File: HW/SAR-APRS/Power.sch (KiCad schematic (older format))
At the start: 22 parts

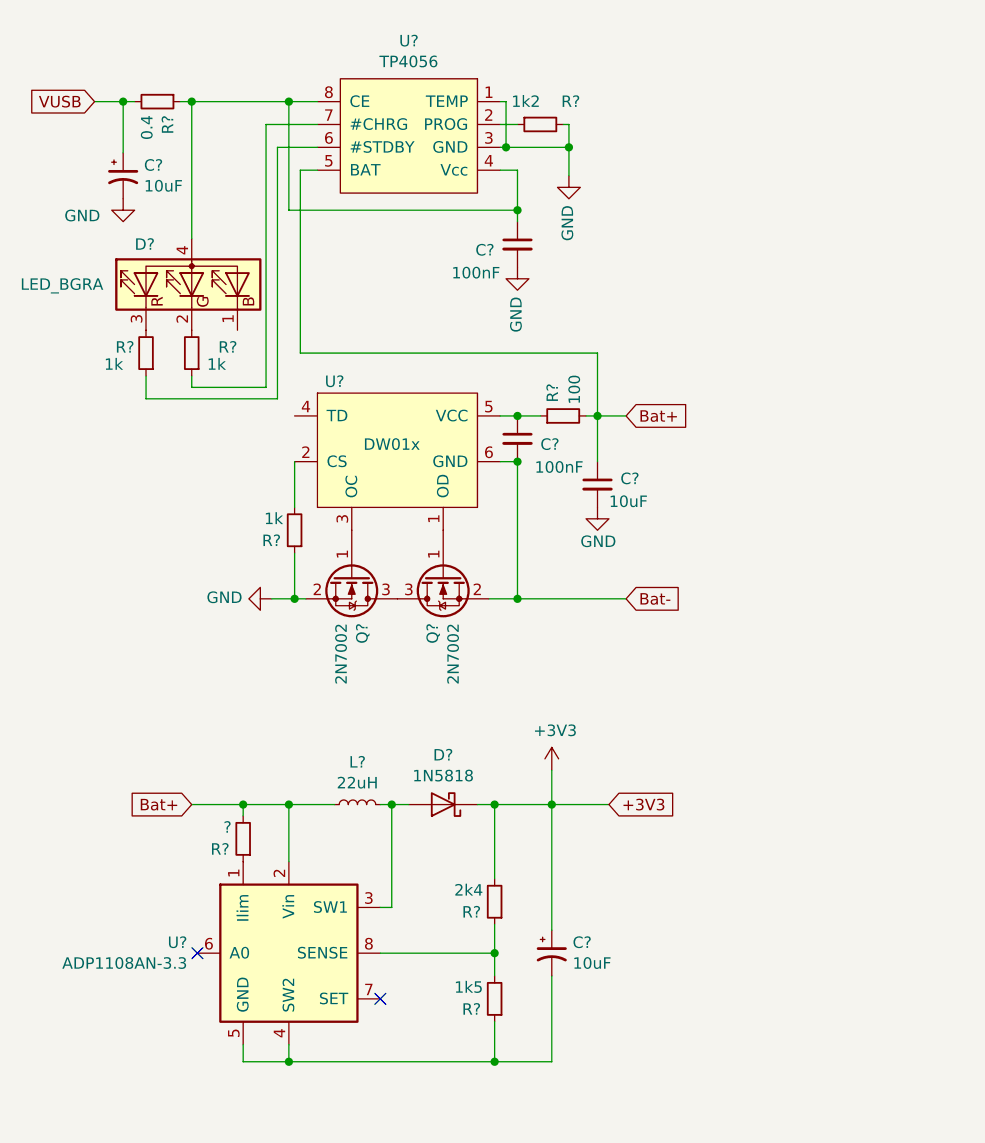
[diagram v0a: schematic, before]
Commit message: schematic update
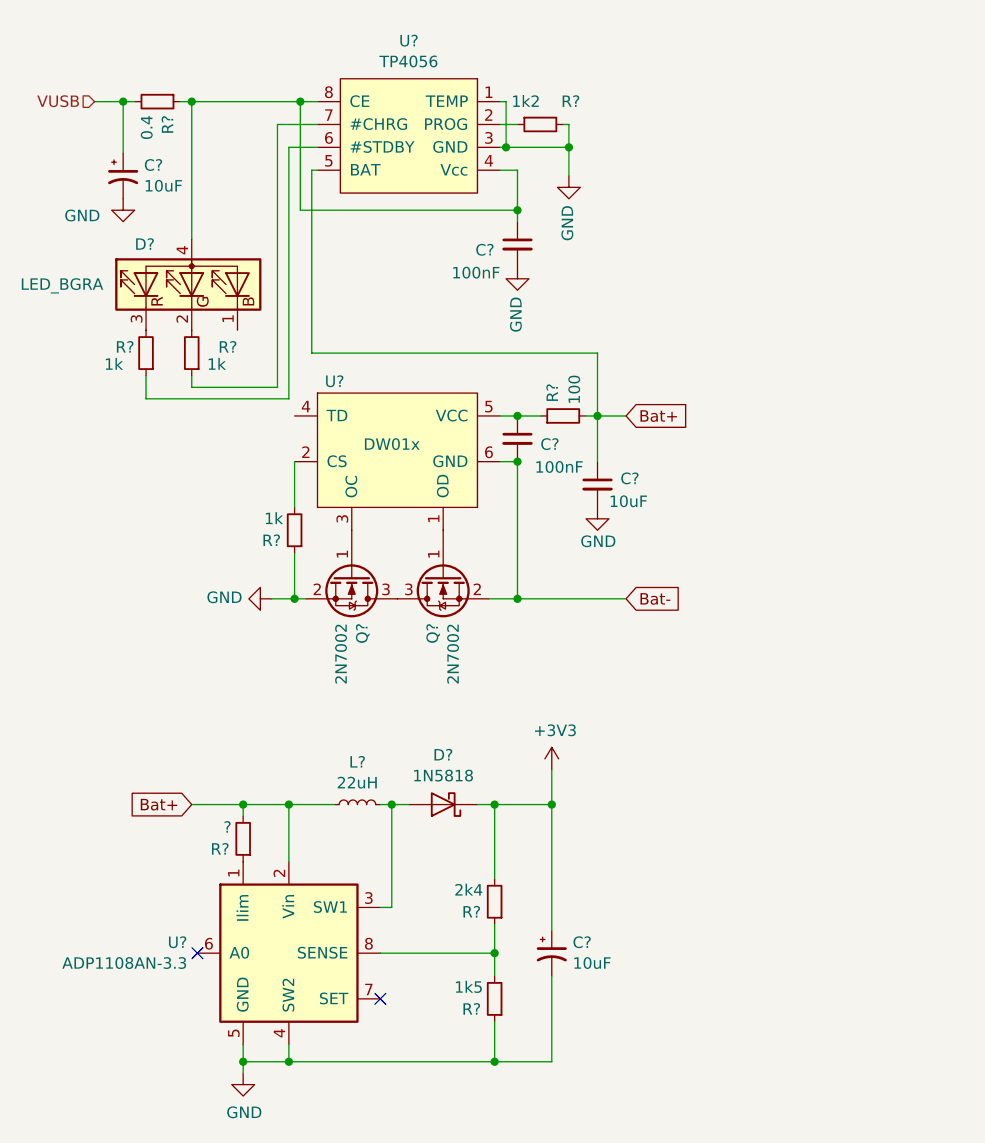
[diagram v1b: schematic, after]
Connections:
- net GND: now also C?.2, R?.1, U?.4 (SW2), U?.5 (GND)
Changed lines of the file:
@@
 	5050 3075 5050 3125
 Wire Wire Line
-	5050 3125 5375 3125
-Wire Wire Line
-	5375 1975 5600 1975
+	5050 3125 5425 3125
+Wire Wire Line
+	5425 1975 5600 1975
 Wire Wire Line
 	4850 3075 4850 3175
 Wire Wire Line
-	4850 3175 5425 3175
-Wire Wire Line
-	5425 2075 5600 2075
+	4850 3175 5475 3175
+Wire Wire Line
+	5475 2075 5600 2075
 $Comp
 L device:C_Small C?
@@
 $EndComp
 Wire Wire Line
-	5050 1875 5475 1875
-Wire Wire Line
-	5375 1975 5375 3125
-Wire Wire Line
-	5425 2075 5425 3175
-Wire Wire Line
-	5475 1875 5475 2350
-Wire Wire Line
-	5475 2350 6475 2350
-Wire Wire Line
-	5475 1875 5600 1875
+	5050 1875 5525 1875
+Wire Wire Line
+	5425 1975 5425 3125
+Wire Wire Line
+	5475 2075 5475 3175
+Wire Wire Line
+	5525 1875 5525 2350
+Wire Wire Line
+	5525 2350 6475 2350
+Wire Wire Line
+	5525 1875 5600 1875
 Wire Wire Line
 	6475 2175 6475 2350
@@
 Wire Wire Line
 	6700 2075 6700 2200
-Connection ~ 5475 1875
-Wire Wire Line
-	5600 2175 5525 2175
-Wire Wire Line
-	5525 2175 5525 2975
-Wire Wire Line
-	5525 2975 6825 2975
+Connection ~ 5525 1875
+Wire Wire Line
+	5600 2175 5575 2175
+Wire Wire Line
+	5575 2175 5575 2975
+Wire Wire Line
+	5575 2975 6825 2975
 Wire Wire Line
 	6825 2975 6825 3250
@@
 Text GLabel 5050 4950 0    50   Input ~ 0
 Bat+
-Text GLabel 4625 1875 0    50   Input ~ 0
-VUSB
 Wire Wire Line
 	4750 1875 4625 1875
 Connection ~ 4750 1875
-Text GLabel 6875 4950 2    50   Input ~ 0
-+3V3
-Wire Wire Line
-	6875 4950 6625 4950
+$Comp
+L power:GND #PWR?
+U 1 1 5C75CEA2
+P 5275 6125
+F 0 "#PWR?" H 5275 5875 50  0001 C CNN
+F 1 "GND" H 5280 5952 50  0000 C CNN
+F 2 "" H 5275 6125 50  0001 C CNN
+F 3 "" H 5275 6125 50  0001 C CNN
+	1    5275 6125
+	1    0    0    -1
+$EndComp
+Wire Wire Line
+	5275 6125 5275 6075
+Connection ~ 5275 6075
+Text HLabel 4625 1875 0    50   Input ~ 0
+VUSB
 $EndSCHEMATC

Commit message: schem and pcb update
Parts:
- R6: renamed from R?; footprint (none) -> Resistors_SMD:R_0805_HandSoldering
- R7: renamed from R?; footprint (none) -> Resistors_SMD:R_0603
- U2: renamed from U?; footprint (none) -> IO:SO-8_3.9x4.9mm_P1.27mm
- U3: renamed from U?; footprint (none) -> Mlab_IO:SOT-23-6
- U4: renamed from U?; footprint Housings_DIP:DIP-8_W7.62mm -> Housings_SOIC:SOIC-8_3.9x4.9mm_Pitch1.27mm
- gave numbers to parts that had none: 17
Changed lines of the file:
@@
 EESchema Schematic File Version 4
 LIBS:SAR-APRS-cache
-EELAYER 28 0
+EELAYER 29 0
 EELAYER END
 $Descr A4 11693 8268
@@
 P 6700 2200
 AR Path="/5C95AC3C" Ref="#PWR?"  Part="1"
-AR Path="/5C948828/5C95AC3C" Ref="#PWR?"  Part="1"
-F 0 "#PWR?" H 6700 1950 50  0001 C CNN
+AR Path="/5C948828/5C95AC3C" Ref="#PWR0115"  Part="1"
+F 0 "#PWR0115" H 6700 1950 50  0001 C CNN
 F 1 "GND" V 6705 2072 50  0000 R CNN
 F 2 "" H 6700 2200 50  0001 C CNN
@@
 P 6575 1975
 AR Path="/5C95AC42" Ref="R?"  Part="1"
-AR Path="/5C948828/5C95AC42" Ref="R?"  Part="1"
-F 0 "R?" V 6475 1800 50  0000 L CNN
+AR Path="/5C948828/5C95AC42" Ref="R7"  Part="1"
+F 0 "R7" V 6475 1800 50  0000 L CNN
 F 1 "1k2" V 6475 1975 50  0000 L CNN
-F 2 "" H 6575 1975 50  0001 C CNN
+F 2 "Resistors_SMD:R_0603" H 6575 1975 50  0001 C CNN
 F 3 "~" H 6575 1975 50  0001 C CNN
 	1    6575 1975
@@
 P 6825 3550
 AR Path="/5C95AC48" Ref="C?"  Part="1"
-AR Path="/5C948828/5C95AC48" Ref="C?"  Part="1"
-F 0 "C?" H 6925 3575 50  0000 L CNN
+AR Path="/5C948828/5C95AC48" Ref="C11"  Part="1"
+F 0 "C11" H 6925 3575 50  0000 L CNN
 F 1 "10uF" H 6875 3475 50  0000 L CNN
 F 2 "" H 6825 3550 50  0001 C CNN
@@
 P 4900 1875
 AR Path="/5C95AC4E" Ref="R?"  Part="1"
-AR Path="/5C948828/5C95AC4E" Ref="R?"  Part="1"
-F 0 "R?" H 4959 1921 50  0000 L CNN
+AR Path="/5C948828/5C95AC4E" Ref="R6"  Part="1"
+F 0 "R6" H 4959 1921 50  0000 L CNN
 F 1 "0.4" H 4959 1830 50  0000 L CNN
-F 2 "" H 4900 1875 50  0001 C CNN
+F 2 "Resistors_SMD:R_0805_HandSoldering" H 4900 1875 50  0001 C CNN
 F 3 "~" H 4900 1875 50  0001 C CNN
 	1    4900 1875
@@
 P 4750 2300
 AR Path="/5C95AC5E" Ref="#PWR?"  Part="1"
-AR Path="/5C948828/5C95AC5E" Ref="#PWR?"  Part="1"
-F 0 "#PWR?" H 4750 2050 50  0001 C CNN
+AR Path="/5C948828/5C95AC5E" Ref="#PWR0116"  Part="1"
+F 0 "#PWR0116" H 4750 2050 50  0001 C CNN
 F 1 "GND" H 4650 2225 50  0000 R CNN
 F 2 "" H 4750 2300 50  0001 C CNN
@@
 P 5050 2975
 AR Path="/5C95AC6D" Ref="R?"  Part="1"
-AR Path="/5C948828/5C95AC6D" Ref="R?"  Part="1"
-F 0 "R?" H 4850 2950 50  0000 L CNN
+AR Path="/5C948828/5C95AC6D" Ref="R9"  Part="1"
+F 0 "R9" H 4850 2950 50  0000 L CNN
 F 1 "1k" H 4900 3025 50  0000 L CNN
 F 2 "" H 5050 2975 50  0001 C CNN
@@
 P 4850 2975
 AR Path="/5C95AC73" Ref="R?"  Part="1"
-AR Path="/5C948828/5C95AC73" Ref="R?"  Part="1"
-F 0 "R?" H 4900 2950 50  0000 L CNN
+AR Path="/5C948828/5C95AC73" Ref="R8"  Part="1"
+F 0 "R8" H 4900 2950 50  0000 L CNN
 F 1 "1k" H 4950 3025 50  0000 L CNN
 F 2 "" H 4850 2975 50  0001 C CNN
@@
 P 5050 2675
 AR Path="/5C95AC7B" Ref="D?"  Part="1"
-AR Path="/5C948828/5C95AC7B" Ref="D?"  Part="1"
-F 0 "D?" V 5225 2925 50  0000 R CNN
+AR Path="/5C948828/5C95AC7B" Ref="D1"  Part="1"
+F 0 "D1" V 5225 2925 50  0000 R CNN
 F 1 "LED_BGRA" V 5050 3425 50  0000 R CNN
 F 2 "" H 5050 2625 50  0001 C CNN
@@
 P 6475 3350
 AR Path="/5C95AC89" Ref="C?"  Part="1"
-AR Path="/5C948828/5C95AC89" Ref="C?"  Part="1"
-F 0 "C?" H 6575 3325 50  0000 L CNN
+AR Path="/5C948828/5C95AC89" Ref="C10"  Part="1"
+F 0 "C10" H 6575 3325 50  0000 L CNN
 F 1 "100nF" H 6550 3225 50  0000 L CNN
 F 2 "" H 6475 3350 50  0001 C CNN
@@
 P 6675 3250
 AR Path="/5C95AC8F" Ref="R?"  Part="1"
-AR Path="/5C948828/5C95AC8F" Ref="R?"  Part="1"
-F 0 "R?" H 6734 3296 50  0000 L CNN
+AR Path="/5C948828/5C95AC8F" Ref="R10"  Part="1"
+F 0 "R10" H 6734 3296 50  0000 L CNN
 F 1 "100" H 6725 3200 50  0000 L CNN
 F 2 "" H 6675 3250 50  0001 C CNN
@@
 P 6150 3950
 AR Path="/5C95AC99" Ref="Q?"  Part="1"
-AR Path="/5C948828/5C95AC99" Ref="Q?"  Part="1"
-F 0 "Q?" H 6356 3996 50  0000 L CNN
+AR Path="/5C948828/5C95AC99" Ref="Q3"  Part="1"
+F 0 "Q3" H 6356 3996 50  0000 L CNN
 F 1 "2N7002" H 6356 3905 50  0000 L CNN
 F 2 "TO_SOT_Packages_SMD:SOT-23" H 6350 3875 50  0001 L CIN
@@
 P 5750 3950
 AR Path="/5C95AC9F" Ref="Q?"  Part="1"
-AR Path="/5C948828/5C95AC9F" Ref="Q?"  Part="1"
-F 0 "Q?" H 5956 3996 50  0000 L CNN
+AR Path="/5C948828/5C95AC9F" Ref="Q2"  Part="1"
+F 0 "Q2" H 5956 3996 50  0000 L CNN
 F 1 "2N7002" H 5956 3905 50  0000 L CNN
 F 2 "TO_SOT_Packages_SMD:SOT-23" H 5950 3875 50  0001 L CIN
@@
 P 5500 3750
 AR Path="/5C95ACA5" Ref="R?"  Part="1"
-AR Path="/5C948828/5C95ACA5" Ref="R?"  Part="1"
-F 0 "R?" H 5559 3796 50  0000 L CNN
+AR Path="/5C948828/5C95ACA5" Ref="R11"  Part="1"
+F 0 "R11" H 5559 3796 50  0000 L CNN
 F 1 "1k" H 5550 3700 50  0000 L CNN
 F 2 "" H 5500 3750 50  0001 C CNN
@@
 P 5950 3350
 AR Path="/5C95ACB0" Ref="U?"  Part="1"
-AR Path="/5C948828/5C95ACB0" Ref="U?"  Part="1"
-F 0 "U?" H 5675 3600 50  0000 C CNN
+AR Path="/5C948828/5C95ACB0" Ref="U3"  Part="1"
+F 0 "U3" H 5675 3600 50  0000 C CNN
 F 1 "DW01x" H 5925 3325 50  0000 C CNN
-F 2 "" H 6000 3250 50  0001 C CNN
+F 2 "Mlab_IO:SOT-23-6" H 6000 3250 50  0001 C CNN
 F 3 "" H 6000 3250 50  0001 C CNN
 	1    5950 3350
@@
 P 6000 2025
 AR Path="/5C95ACB6" Ref="U?"  Part="1"
-AR Path="/5C948828/5C95ACB6" Ref="U?"  Part="1"
-F 0 "U?" H 6000 2440 50  0000 C CNN
+AR Path="/5C948828/5C95ACB6" Ref="U2"  Part="1"
+F 0 "U2" H 6000 2440 50  0000 C CNN
 F 1 "TP4056" H 6000 2349 50  0000 C CNN
-F 2 "" H 5450 2425 50  0001 C CNN
+F 2 "IO:SO-8_3.9x4.9mm_P1.27mm" H 5450 2425 50  0001 C CNN
 F 3 "" H 5450 2425 50  0001 C CNN
 	1    6000 2025
@@
 P 6475 2500
 AR Path="/5C95ACC1" Ref="C?"  Part="1"
-AR Path="/5C948828/5C95ACC1" Ref="C?"  Part="1"
-F 0 "C?" H 6575 2475 50  0000 L CNN
+AR Path="/5C948828/5C95ACC1" Ref="C9"  Part="1"
+F 0 "C9" H 6575 2475 50  0000 L CNN
 F 1 "100nF" H 6550 2375 50  0000 L CNN
 F 2 "" H 6475 2500 50  0001 C CNN
@@
 P 6475 2600
 AR Path="/5C95ACC8" Ref="#PWR?"  Part="1"
-AR Path="/5C948828/5C95ACC8" Ref="#PWR?"  Part="1"
-F 0 "#PWR?" H 6475 2350 50  0001 C CNN
+AR Path="/5C948828/5C95ACC8" Ref="#PWR0117"  Part="1"
+F 0 "#PWR0117" H 6475 2350 50  0001 C CNN
 F 1 "GND" V 6480 2472 50  0000 R CNN
 F 2 "" H 6475 2600 50  0001 C CNN
@@
 P 5400 4050
 AR Path="/5C95ACE6" Ref="#PWR?"  Part="1"
-AR Path="/5C948828/5C95ACE6" Ref="#PWR?"  Part="1"
-F 0 "#PWR?" H 5400 3800 50  0001 C CNN
+AR Path="/5C948828/5C95ACE6" Ref="#PWR0118"  Part="1"
+F 0 "#PWR0118" H 5400 3800 50  0001 C CNN
 F 1 "GND" V 5405 3922 50  0000 R CNN
 F 2 "" H 5400 4050 50  0001 C CNN
@@
 P 6825 3650
 AR Path="/5C95ACF0" Ref="#PWR?"  Part="1"
-AR Path="/5C948828/5C95ACF0" Ref="#PWR?"  Part="1"
-F 0 "#PWR?" H 6825 3400 50  0001 C CNN
+AR Path="/5C948828/5C95ACF0" Ref="#PWR0119"  Part="1"
+F 0 "#PWR0119" H 6825 3400 50  0001 C CNN
 F 1 "GND" H 6900 3500 50  0000 R CNN
 F 2 "" H 6825 3650 50  0001 C CNN
@@
 P 5475 5600
 AR Path="/5C95ACF6" Ref="U?"  Part="1"
-AR Path="/5C948828/5C95ACF6" Ref="U?"  Part="1"
-F 0 "U?" H 5031 5646 50  0000 R CNN
+AR Path="/5C948828/5C95ACF6" Ref="U4"  Part="1"
+F 0 "U4" H 5031 5646 50  0000 R CNN
 F 1 "ADP1108AN-3.3" H 5031 5555 50  0000 R CNN
-F 2 "Housings_DIP:DIP-8_W7.62mm" H 5525 5250 50  0001 L CNN
+F 2 "Housings_SOIC:SOIC-8_3.9x4.9mm_Pitch1.27mm" H 5525 5250 50  0001 L CNN
 F 3 "http://www.analog.com/media/en/technical-documentation/data-sheets/ADP1108.pdf" H 5275 6200 50  0001 C CNN
 	1    5475 5600
@@
 P 6150 4950
 AR Path="/5C95ACFC" Ref="D?"  Part="1"
-AR Path="/5C948828/5C95ACFC" Ref="D?"  Part="1"
-F 0 "D?" H 6150 4734 50  0000 C CNN
+AR Path="/5C948828/5C95ACFC" Ref="D2"  Part="1"
+F 0 "D2" H 6150 4734 50  0000 C CNN
 F 1 "1N5818" H 6150 4825 50  0000 C CNN
 F 2 "Diode_THT:D_DO-41_SOD81_P10.16mm_Horizontal" H 6150 4775 50  0001 C CNN
@@
 P 5775 4950
 AR Path="/5C95AD02" Ref="L?"  Part="1"
-AR Path="/5C948828/5C95AD02" Ref="L?"  Part="1"
-F 0 "L?" V 5960 4950 50  0000 C CNN
+AR Path="/5C948828/5C95AD02" Ref="L4"  Part="1"
+F 0 "L4" V 5960 4950 50  0000 C CNN
 F 1 "22uH" V 5869 4950 50  0000 C CNN
 F 2 "" H 5775 4950 50  0001 C CNN
@@
 P 5275 5100
 AR Path="/5C95AD08" Ref="R?"  Part="1"
-AR Path="/5C948828/5C95AD08" Ref="R?"  Part="1"
-F 0 "R?" H 5334 5146 50  0000 L CNN
+AR Path="/5C948828/5C95AD08" Ref="R12"  Part="1"
+F 0 "R12" H 5334 5146 50  0000 L CNN
 F 1 "?" H 5325 5050 50  0000 L CNN
 F 2 "" H 5275 5100 50  0001 C CNN
@@
 P 6375 5800
 AR Path="/5C95AD18" Ref="R?"  Part="1"
-AR Path="/5C948828/5C95AD18" Ref="R?"  Part="1"
-F 0 "R?" H 6434 5846 50  0000 L CNN
+AR Path="/5C948828/5C95AD18" Ref="R14"  Part="1"
+F 0 "R14" H 6434 5846 50  0000 L CNN
 F 1 "1k5" H 6425 5750 50  0000 L CNN
 F 2 "" H 6375 5800 50  0001 C CNN
@@
 P 6375 5375
 AR Path="/5C95AD1E" Ref="R?"  Part="1"
-AR Path="/5C948828/5C95AD1E" Ref="R?"  Part="1"
-F 0 "R?" H 6434 5421 50  0000 L CNN
+AR Path="/5C948828/5C95AD1E" Ref="R13"  Part="1"
+F 0 "R13" H 6434 5421 50  0000 L CNN
 F 1 "2k4" H 6425 5325 50  0000 L CNN
 F 2 "" H 6375 5375 50  0001 C CNN
@@
 P 4750 2200
 AR Path="/5C95AD30" Ref="C?"  Part="1"
-AR Path="/5C948828/5C95AD30" Ref="C?"  Part="1"
-F 0 "C?" H 4841 2246 50  0000 L CNN
+AR Path="/5C948828/5C95AD30" Ref="C8"  Part="1"
+F 0 "C8" H 4841 2246 50  0000 L CNN
 F 1 "10uF" H 4841 2155 50  0000 L CNN
 F 2 "" H 4750 2200 50  0001 C CNN
@@
 P 6625 5600
 AR Path="/5C95AD36" Ref="C?"  Part="1"
-AR Path="/5C948828/5C95AD36" Ref="C?"  Part="1"
-F 0 "C?" H 6716 5646 50  0000 L CNN
+AR Path="/5C948828/5C95AD36" Ref="C12"  Part="1"
+F 0 "C12" H 6716 5646 50  0000 L CNN
 F 1 "10uF" H 6716 5555 50  0000 L CNN
 F 2 "" H 6625 5600 50  0001 C CNN
@@
 P 6625 4800
 AR Path="/5C95AD42" Ref="#PWR?"  Part="1"
-AR Path="/5C948828/5C95AD42" Ref="#PWR?"  Part="1"
-F 0 "#PWR?" H 6625 4650 50  0001 C CNN
+AR Path="/5C948828/5C95AD42" Ref="#PWR0120"  Part="1"
+F 0 "#PWR0120" H 6625 4650 50  0001 C CNN
 F 1 "+3V3" H 6640 4973 50  0000 C CNN
 F 2 "" H 6625 4800 50  0001 C CNN
@@
 Connection ~ 4750 1875
 $Comp
-L power:GND #PWR?
+L power:GND #PWR0121
 U 1 1 5C75CEA2
 P 5275 6125
-F 0 "#PWR?" H 5275 5875 50  0001 C CNN
+F 0 "#PWR0121" H 5275 5875 50  0001 C CNN
 F 1 "GND" H 5280 5952 50  0000 C CNN
 F 2 "" H 5275 6125 50  0001 C CNN

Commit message: schm and pcb update
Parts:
- removed D1: LED_BGRA, symbol device:LED_BGRA
- added D1, D2: LED, LEDs:LED_0603, symbol device:LED
- C10, C9: footprint (none) -> Capacitors_SMD:C_0603
- R10, R11, R8, R9: footprint (none) -> Resistors_SMD:R_0603
- R6: footprint Resistors_SMD:R_0805_HandSoldering -> Resistors_SMD:R_2512
- renumbered D2 to D3
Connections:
- net at C9.1, R6.1, U2.4 (Vcc)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: now also D1.2 (A), D2.2 (A)
- net at R9.2: now also D2.1 (K)
- net at R8.2: now also D1.1 (K)
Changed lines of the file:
@@
 F 0 "R6" H 4959 1921 50  0000 L CNN
 F 1 "0.4" H 4959 1830 50  0000 L CNN
-F 2 "Resistors_SMD:R_0805_HandSoldering" H 4900 1875 50  0001 C CNN
+F 2 "Resistors_SMD:R_2512" H 4900 1875 50  0001 C CNN
 F 3 "~" H 4900 1875 50  0001 C CNN
 	1    4900 1875
@@
 F 0 "R9" H 4850 2950 50  0000 L CNN
 F 1 "1k" H 4900 3025 50  0000 L CNN
-F 2 "" H 5050 2975 50  0001 C CNN
+F 2 "Resistors_SMD:R_0603" H 5050 2975 50  0001 C CNN
 F 3 "~" H 5050 2975 50  0001 C CNN
 	1    5050 2975
@@
 F 0 "R8" H 4900 2950 50  0000 L CNN
 F 1 "1k" H 4950 3025 50  0000 L CNN
-F 2 "" H 4850 2975 50  0001 C CNN
+F 2 "Resistors_SMD:R_0603" H 4850 2975 50  0001 C CNN
 F 3 "~" H 4850 2975 50  0001 C CNN
 	1    4850 2975
 	-1   0    0    1
 $EndComp
-Wire Wire Line
-	5050 2475 5050 1875
 Connection ~ 5050 1875
-$Comp
-L device:LED_BGRA D?
-U 1 1 5C95AC7B
-P 5050 2675
-AR Path="/5C95AC7B" Ref="D?"  Part="1"
-AR Path="/5C948828/5C95AC7B" Ref="D1"  Part="1"
-F 0 "D1" V 5225 2925 50  0000 R CNN
-F 1 "LED_BGRA" V 5050 3425 50  0000 R CNN
-F 2 "" H 5050 2625 50  0001 C CNN
-F 3 "~" H 5050 2625 50  0001 C CNN
-	1    5050 2675
-	0    -1   -1   0
-$EndComp
 Wire Wire Line
 	5050 3075 5050 3125
@@
 F 0 "C10" H 6575 3325 50  0000 L CNN
 F 1 "100nF" H 6550 3225 50  0000 L CNN
-F 2 "" H 6475 3350 50  0001 C CNN
+F 2 "Capacitors_SMD:C_0603" H 6475 3350 50  0001 C CNN
 F 3 "~" H 6475 3350 50  0001 C CNN
 	1    6475 3350
@@
 F 0 "R10" H 6734 3296 50  0000 L CNN
 F 1 "100" H 6725 3200 50  0000 L CNN
-F 2 "" H 6675 3250 50  0001 C CNN
+F 2 "Resistors_SMD:R_0603" H 6675 3250 50  0001 C CNN
 F 3 "~" H 6675 3250 50  0001 C CNN
 	1    6675 3250
@@
 F 0 "R11" H 5559 3796 50  0000 L CNN
 F 1 "1k" H 5550 3700 50  0000 L CNN
-F 2 "" H 5500 3750 50  0001 C CNN
+F 2 "Resistors_SMD:R_0603" H 5500 3750 50  0001 C CNN
 F 3 "~" H 5500 3750 50  0001 C CNN
 	1    5500 3750
@@
 F 0 "C9" H 6575 2475 50  0000 L CNN
 F 1 "100nF" H 6550 2375 50  0000 L CNN
-F 2 "" H 6475 2500 50  0001 C CNN
+F 2 "Capacitors_SMD:C_0603" H 6475 2500 50  0001 C CNN
 F 3 "~" H 6475 2500 50  0001 C CNN
 	1    6475 2500
@@
 P 6150 4950
 AR Path="/5C95ACFC" Ref="D?"  Part="1"
-AR Path="/5C948828/5C95ACFC" Ref="D2"  Part="1"
-F 0 "D2" H 6150 4734 50  0000 C CNN
+AR Path="/5C948828/5C95ACFC" Ref="D3"  Part="1"
+F 0 "D3" H 6150 4734 50  0000 C CNN
 F 1 "1N5818" H 6150 4825 50  0000 C CNN
 F 2 "Diode_THT:D_DO-41_SOD81_P10.16mm_Horizontal" H 6150 4775 50  0001 C CNN
@@
 Text HLabel 4625 1875 0    50   Input ~ 0
 VUSB
+$Comp
+L device:LED D1
+U 1 1 5CA40B18
+P 4850 2725
+F 0 "D1" V 4925 2900 50  0000 R CNN
+F 1 "LED" V 4825 2950 50  0000 R CNN
+F 2 "LEDs:LED_0603" H 4850 2725 50  0001 C CNN
+F 3 "~" H 4850 2725 50  0001 C CNN
+	1    4850 2725
+	0    -1   -1   0
+$EndComp
+$Comp
+L device:LED D2
+U 1 1 5CA42099
+P 5050 2725
+F 0 "D2" V 5089 2608 50  0000 R CNN
+F 1 "LED" V 4998 2608 50  0000 R CNN
+F 2 "LEDs:LED_0603" H 5050 2725 50  0001 C CNN
+F 3 "~" H 5050 2725 50  0001 C CNN
+	1    5050 2725
+	0    -1   -1   0
+$EndComp
+Wire Wire Line
+	4850 2575 4850 2525
+Wire Wire Line
+	4850 2525 5050 2525
+Wire Wire Line
+	5050 1875 5050 2525
+Wire Wire Line
+	5050 2575 5050 2525
+Connection ~ 5050 2525
 $EndSCHEMATC
